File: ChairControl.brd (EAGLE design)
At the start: 150 x 84 mm, 34 parts, among them J1 Digital_0_7, J2 Analog, J3 Digital_8_13, J4 Analog, J5 Digital_0_7, SW1 SWITCH-DPDT3, X1 INPUT, X2 OUTPUT, X4 INPUT

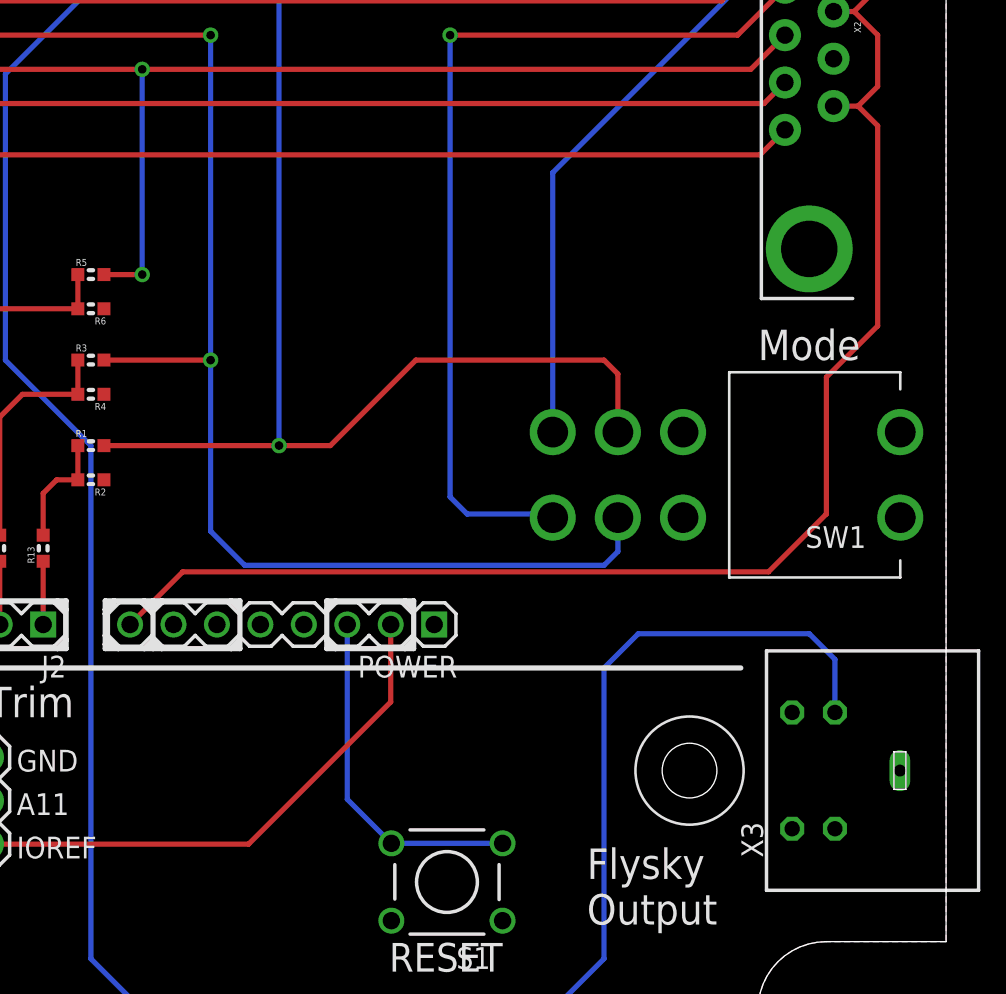
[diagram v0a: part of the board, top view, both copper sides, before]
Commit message: Isolated 12V power from passthrough to allow separate power source
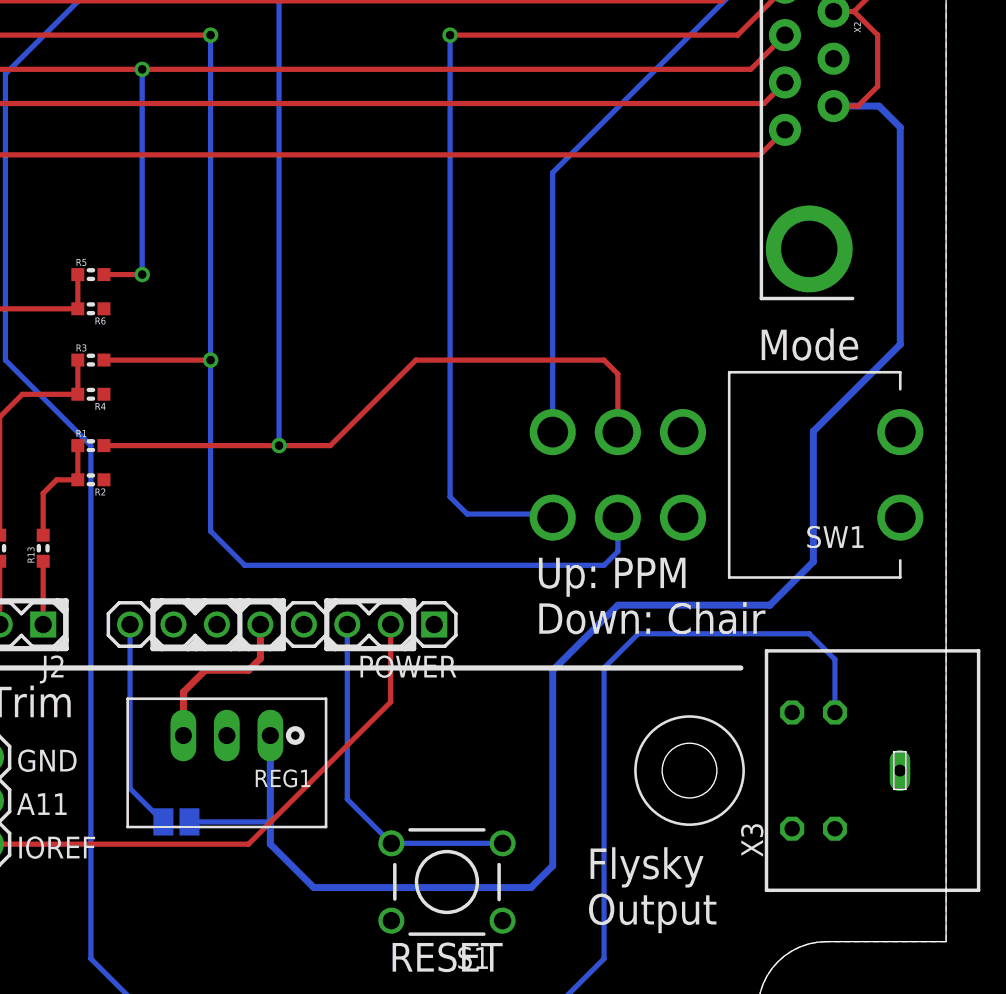
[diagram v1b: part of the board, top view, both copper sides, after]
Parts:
- added REG1: K7805-500R3, freetronics-jon:K78XX-500R3
- added SJ1: (no value), freetronics-jon:SJ
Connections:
- new net VIN: POWER.8, SJ1.1
- net 12V: now also REG1.1, SJ1.2; no longer POWER.8
- net 5V: now also REG1.3
- net GND: now also REG1.2
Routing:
- net 12V: track 291.5 -> 313.0 mm
- net VIN: track 0.00 -> 12.3 mm
- net 5V: track 0.00 -> 9.84 mm
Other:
- board text added: "Up: PPM Down: Chair"
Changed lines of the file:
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@@
 <?xml version="1.0" encoding="utf-8"?>
 <!DOCTYPE eagle SYSTEM "eagle.dtd">
-<eagle version="8.6.0">
+<eagle version="8.7.0">
 <drawing>
 <settings>
@@
 <setting verticaltext="up"/>
 </settings>
-<grid distance="0.05" unitdist="inch" unit="inch" style="lines" multiple="1" display="yes" altdistance="0.005" altunitdist="inch" altunit="inch"/>
+<grid distance="1" unitdist="mm" unit="mm" style="lines" multiple="1" display="yes" altdistance="0.005" altunitdist="inch" altunit="inch"/>
 <layers>
 <layer number="1" name="Top" color="4" fill="1" visible="yes" active="yes"/>
@@
 <wire x1="75.184" y1="24.13" x2="75.692" y2="24.638" width="0.3048" layer="21"/>
 <wire x1="75.692" y1="26.416" x2="75.184" y2="26.924" width="0.3048" layer="21"/>
-<wire x1="100.838" y1="26.924" x2="100.838" y2="26.416" width="0.3048" layer="21"/>
-<wire x1="100.838" y1="26.162" x2="100.838" y2="24.892" width="0.3048" layer="21"/>
-<wire x1="100.838" y1="24.384" x2="100.838" y2="24.13" width="0.3048" layer="21"/>
-<wire x1="100.838" y1="24.13" x2="101.6" y2="24.13" width="0.3048" layer="21"/>
-<wire x1="101.6" y1="24.13" x2="103.124" y2="24.13" width="0.3048" layer="21"/>
-<wire x1="103.124" y1="24.13" x2="103.632" y2="24.13" width="0.3048" layer="21"/>
 <wire x1="103.632" y1="24.13" x2="103.632" y2="24.638" width="0.3048" layer="21"/>
 <wire x1="103.632" y1="24.638" x2="103.632" y2="26.416" width="0.3048" layer="21"/>
 <wire x1="103.632" y1="26.416" x2="103.632" y2="26.924" width="0.3048" layer="21"/>
-<wire x1="103.632" y1="26.924" x2="103.124" y2="26.924" width="0.3048" layer="21"/>
-<wire x1="103.124" y1="26.924" x2="101.346" y2="26.924" width="0.3048" layer="21"/>
-<wire x1="101.346" y1="26.924" x2="100.838" y2="26.924" width="0.3048" layer="21"/>
-<wire x1="101.346" y1="26.924" x2="100.838" y2="26.416" width="0.3048" layer="21"/>
-<wire x1="100.838" y1="26.416" x2="100.838" y2="26.162" width="0.3048" layer="21"/>
-<wire x1="100.838" y1="26.162" x2="101.346" y2="26.67" width="0.3048" layer="21"/>
-<wire x1="103.124" y1="26.924" x2="103.632" y2="26.416" width="0.3048" layer="21"/>
-<wire x1="103.124" y1="24.13" x2="103.632" y2="24.638" width="0.3048" layer="21"/>
-<wire x1="101.6" y1="24.13" x2="100.838" y2="24.892" width="0.3048" layer="21"/>
-<wire x1="100.838" y1="24.892" x2="100.838" y2="24.384" width="0.3048" layer="21"/>
-<wire x1="100.838" y1="24.384" x2="101.092" y2="24.384" width="0.3048" layer="21"/>
 <wire x1="113.792" y1="26.924" x2="113.792" y2="26.416" width="0.3048" layer="21"/>
 <wire x1="113.792" y1="26.416" x2="113.792" y2="24.638" width="0.3048" layer="21"/>
@@
 <wire x1="118.872" y1="26.416" x2="118.364" y2="26.924" width="0.3048" layer="21"/>
 <wire x1="103.632" y1="26.924" x2="104.14" y2="26.924" width="0.3048" layer="21"/>
-<wire x1="104.14" y1="26.924" x2="108.204" y2="26.924" width="0.3048" layer="21"/>
+<wire x1="104.14" y1="26.924" x2="105.664" y2="26.924" width="0.3048" layer="21"/>
+<wire x1="105.664" y1="26.924" x2="106.68" y2="26.924" width="0.3048" layer="21"/>
+<wire x1="106.68" y1="26.924" x2="108.204" y2="26.924" width="0.3048" layer="21"/>
 <wire x1="108.204" y1="26.924" x2="108.712" y2="26.924" width="0.3048" layer="21"/>
 <wire x1="108.712" y1="26.924" x2="108.712" y2="26.416" width="0.3048" layer="21"/>
@@
 <wire x1="108.712" y1="24.638" x2="108.712" y2="24.13" width="0.3048" layer="21"/>
 <wire x1="108.712" y1="24.13" x2="108.204" y2="24.13" width="0.3048" layer="21"/>
-<wire x1="108.204" y1="24.13" x2="104.14" y2="24.13" width="0.3048" layer="21"/>
+<wire x1="108.204" y1="24.13" x2="106.68" y2="24.13" width="0.3048" layer="21"/>
+<wire x1="106.68" y1="24.13" x2="106.172" y2="24.13" width="0.3048" layer="21"/>
+<wire x1="105.664" y1="24.13" x2="104.14" y2="24.13" width="0.3048" layer="21"/>
 <wire x1="104.14" y1="24.13" x2="103.632" y2="24.13" width="0.3048" layer="21"/>
 <wire x1="108.204" y1="26.924" x2="108.712" y2="26.416" width="0.3048" layer="21"/>
@@
 <wire x1="103.632" y1="24.638" x2="104.14" y2="24.13" width="0.3048" layer="21"/>
 <wire x1="104.14" y1="26.924" x2="103.632" y2="26.416" width="0.3048" layer="21"/>
+<wire x1="108.712" y1="26.924" x2="109.22" y2="26.924" width="0.3048" layer="21"/>
+<wire x1="109.22" y1="26.924" x2="110.744" y2="26.924" width="0.3048" layer="21"/>
+<wire x1="110.744" y1="26.924" x2="111.252" y2="26.924" width="0.3048" layer="21"/>
+<wire x1="111.252" y1="26.924" x2="111.252" y2="26.416" width="0.3048" layer="21"/>
+<wire x1="111.252" y1="26.416" x2="111.252" y2="24.13" width="0.3048" layer="21"/>
+<wire x1="111.252" y1="24.13" x2="110.49" y2="24.13" width="0.3048" layer="21"/>
+<wire x1="110.49" y1="24.13" x2="109.22" y2="24.13" width="0.3048" layer="21"/>
+<wire x1="109.22" y1="24.13" x2="108.712" y2="24.13" width="0.3048" layer="21"/>
+<wire x1="108.712" y1="26.416" x2="109.22" y2="26.924" width="0.3048" layer="21"/>
+<wire x1="110.744" y1="26.924" x2="111.252" y2="26.416" width="0.3048" layer="21"/>
+<wire x1="108.712" y1="24.638" x2="109.22" y2="24.13" width="0.3048" layer="21"/>
+<wire x1="110.49" y1="24.13" x2="110.744" y2="24.384" width="0.3048" layer="21"/>
+<wire x1="110.744" y1="24.384" x2="110.998" y2="24.638" width="0.3048" layer="21"/>
+<wire x1="110.998" y1="24.638" x2="110.998" y2="24.384" width="0.3048" layer="21"/>
+<wire x1="110.998" y1="24.384" x2="110.744" y2="24.384" width="0.3048" layer="21"/>
+<wire x1="106.68" y1="26.924" x2="106.426" y2="26.67" width="0.3048" layer="21"/>
+<wire x1="106.426" y1="26.67" x2="106.172" y2="26.416" width="0.3048" layer="21"/>
+<wire x1="106.172" y1="26.416" x2="105.918" y2="26.67" width="0.3048" layer="21"/>
+<wire x1="105.664" y1="26.924" x2="105.918" y2="26.67" width="0.3048" layer="21"/>
+<wire x1="105.918" y1="26.67" x2="106.426" y2="26.67" width="0.3048" layer="21"/>
+<wire x1="106.68" y1="24.13" x2="106.172" y2="24.638" width="0.3048" layer="21"/>
+<wire x1="106.172" y1="24.638" x2="105.664" y2="24.13" width="0.3048" layer="21"/>
+<wire x1="105.664" y1="24.13" x2="106.172" y2="24.13" width="0.3048" layer="21"/>
+<wire x1="106.172" y1="24.13" x2="106.172" y2="24.384" width="0.3048" layer="21"/>
+<text x="126" y="25" size="1.778" layer="21" font="vector" ratio="18">Up: PPM
+Down: Chair</text>
 </plain>
 <attributes>
@@
 <element name="JP4" library="freetronics-jon" package="1X03" value="" x="93.98" y="12.7" rot="R90"/>
 <element name="J5" library="freetronics" package="1X08" value="Digital_0_7" x="61.65" y="73.8"/>
+<element name="REG1" library="freetronics-jon" package="K78XX-500R3" value="K7805-500R3" x="107.95" y="19.05" rot="R180"/>
+<element name="SJ1" library="freetronics-jon" package="SJ" value="" x="105" y="14" rot="MR180"/>
 </elements>
 <signals>
@@
 <signal name="5V">
 <contactref element="POWER" pad="5"/>
+<contactref element="REG1" pad="3"/>
+<wire x1="105.41" y1="19.05" x2="105.41" y2="21.59" width="0.4064" layer="1"/>
+<wire x1="105.41" y1="21.59" x2="106.68" y2="22.86" width="0.4064" layer="1"/>
+<wire x1="106.68" y1="22.86" x2="109.22" y2="22.86" width="0.4064" layer="1"/>
+<wire x1="109.22" y1="22.86" x2="109.91" y2="23.55" width="0.4064" layer="1"/>
+<wire x1="109.91" y1="23.55" x2="109.91" y2="25.54" width="0.4064" layer="1"/>
 </signal>
 <signal name="RESET">
@@
 <contactref element="JP2" pad="3"/>
 <contactref element="JP1" pad="3"/>
+<contactref element="REG1" pad="2"/>
 </signal>
 <signal name="SDA">
@@
 <contactref element="X1" pad="9"/>
 <contactref element="X2" pad="9"/>
-<contactref element="POWER" pad="8"/>
 <contactref element="X4" pad="9"/>
 <contactref element="X4" pad="7"/>
@@
 <wire x1="137" y1="71" x2="140" y2="68" width="0.3048" layer="1"/>
 <wire x1="146" y1="67" x2="146" y2="62.76" width="0.3048" layer="1"/>
-<wire x1="143" y1="32" x2="143" y2="40" width="0.3048" layer="1"/>
-<wire x1="143" y1="40" x2="146" y2="43" width="0.3048" layer="1"/>
-<wire x1="146" y1="43" x2="146" y2="54.7" width="0.3048" layer="1"/>
-<wire x1="146" y1="54.7" x2="144.85" y2="55.85" width="0.3048" layer="1"/>
-<wire x1="143" y1="32" x2="139.62" y2="28.62" width="0.3048" layer="1"/>
-<wire x1="139.62" y1="28.62" x2="105.37" y2="28.62" width="0.3048" layer="1"/>
-<wire x1="105.37" y1="28.62" x2="102.29" y2="25.54" width="0.3048" layer="1"/>
+<contactref element="REG1" pad="1"/>
+<wire x1="110.49" y1="12.7" x2="113.03" y2="10.16" width="0.4064" layer="16"/>
+<wire x1="113.03" y1="10.16" x2="125.73" y2="10.16" width="0.4064" layer="16"/>
+<wire x1="125.73" y1="10.16" x2="127" y2="11.43" width="0.4064" layer="16"/>
+<wire x1="127" y1="11.43" x2="127" y2="22.86" width="0.4064" layer="16"/>
+<wire x1="127" y1="22.86" x2="130.81" y2="26.67" width="0.4064" layer="16"/>
+<wire x1="130.81" y1="26.67" x2="139.7" y2="26.67" width="0.4064" layer="16"/>
+<wire x1="139.7" y1="26.67" x2="142.24" y2="29.21" width="0.4064" layer="16"/>
+<wire x1="142.24" y1="29.21" x2="142.24" y2="36.83" width="0.4064" layer="16"/>
+<wire x1="142.24" y1="36.83" x2="147.32" y2="41.91" width="0.4064" layer="16"/>
+<wire x1="147.32" y1="41.91" x2="147.32" y2="54.61" width="0.4064" layer="16"/>
+<wire x1="147.32" y1="54.61" x2="146.08" y2="55.85" width="0.4064" layer="16"/>
+<wire x1="146.08" y1="55.85" x2="143.42" y2="55.85" width="0.4064" layer="16"/>
+<wire x1="110.49" y1="19.05" x2="110.49" y2="14" width="0.4064" layer="16"/>
+<contactref element="SJ1" pad="2"/>
+<wire x1="110.49" y1="14" x2="110.49" y2="12.7" width="0.4064" layer="16"/>
+<wire x1="105.762" y1="14" x2="110.49" y2="14" width="0.3048" layer="16"/>
 </signal>
 <signal name="SPEED_IN_2">
@@
 <wire x1="67.31" y1="20.32" x2="69.27" y2="22.28" width="0.3048" layer="16"/>
 </signal>
+<signal name="VIN">
+<contactref element="POWER" pad="8"/>
+<contactref element="SJ1" pad="1"/>
+<wire x1="104.238" y1="14" x2="102.29" y2="15.948" width="0.3048" layer="16"/>
+<wire x1="102.29" y1="15.948" x2="102.29" y2="25.54" width="0.3048" layer="16"/>
+</signal>
 </signals>
